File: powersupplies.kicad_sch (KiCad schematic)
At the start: 24 parts, among them U1 OB2222M, U2 LM317L_SOT-89

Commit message: All parts on. Set foots for everything. Time to try a layout.
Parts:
- C1, C2, C9: footprint (none) -> Capacitor_SMD:C_0603_1608Metric
- C11, C12: footprint (none) -> Capacitor_SMD:C_0402_1005Metric
- C3: footprint (none) -> Capacitor_SMD:C_0805_2012Metric
- C5, C6, C7: footprint (none) -> Capacitor_THT:CP_Radial_D6.3mm_P2.50mm
- D1, D3: footprint (none) -> Diode_SMD:D_SMF
- D2, D5: footprint (none) -> Diode_SMD:D_SOD-123F
- L1: footprint (none) -> Inductor_THT:L_Axial_L9.5mm_D4.0mm_P5.08mm_Vertical_Fastron_SMCC
- L2: footprint (none) -> Inductor_THT:L_Radial_D8.7mm_P5.00mm_Fastron_07HCP
- R1, R3: footprint (none) -> Resistor_SMD:R_0805_2012Metric
- R2, R26, R4, R9: footprint (none) -> Resistor_SMD:R_0603_1608Metric
- R5: footprint (none) -> Resistor_SMD:R_1206_3216Metric
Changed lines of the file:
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@@
 			)
 		)
-		(property "Footprint" ""
+		(property "Footprint" "Capacitor_SMD:C_0805_2012Metric"
 			(at 100.0252 59.69 0)
 			(effects
@@
 			)
 		)
-		(property "Footprint" ""
+		(property "Footprint" "Resistor_SMD:R_0805_2012Metric"
 			(at 92.456 48.006 90)
 			(effects
@@
 			)
 		)
-		(property "Footprint" ""
+		(property "Footprint" "Diode_SMD:D_SOD-123F"
 			(at 40.64 71.12 0)
 			(effects
@@
 			)
 		)
-		(property "Footprint" ""
+		(property "Footprint" "Diode_SMD:D_SMF"
 			(at 139.7 91.44 0)
 			(effects
@@
 			)
 		)
-		(property "Footprint" ""
+		(property "Footprint" "Capacitor_THT:CP_Radial_D6.3mm_P2.50mm"
 			(at 73.66 80.01 0)
 			(effects
@@
 			)
 		)
-		(property "Footprint" ""
+		(property "Footprint" "Capacitor_SMD:C_0603_1608Metric"
 			(at 186.9948 143.51 0)
 			(effects
@@
 			)
 		)
-		(property "Footprint" ""
+		(property "Footprint" "Capacitor_SMD:C_0603_1608Metric"
 			(at 145.0848 73.66 0)
 			(effects
@@
 			)
 		)
-		(property "Footprint" ""
+		(property "Footprint" "Diode_SMD:D_SMF"
 			(at 157.48 71.12 0)
 			(effects
@@
 			)
 		)
-		(property "Footprint" ""
+		(property "Footprint" "Inductor_THT:L_Axial_L9.5mm_D4.0mm_P5.08mm_Vertical_Fastron_SMCC"
 			(at 67.31 71.12 0)
 			(effects
@@
 			)
 		)
-		(property "Footprint" ""
+		(property "Footprint" "Capacitor_THT:CP_Radial_D6.3mm_P2.50mm"
 			(at 167.64 91.44 0)
 			(effects
@@
 			)
 		)
-		(property "Footprint" ""
+		(property "Footprint" "Capacitor_SMD:C_0603_1608Metric"
 			(at 131.7752 81.28 0)
 			(effects
@@
 			)
 		)
-		(property "Footprint" ""
+		(property "Footprint" "Resistor_SMD:R_0603_1608Metric"
 			(at 139.954 70.104 90)
 			(effects
@@
 			)
 		)
-		(property "Footprint" ""
+		(property "Footprint" "Resistor_SMD:R_1206_3216Metric"
 			(at 125.476 77.724 90)
 			(effects
@@
 			)
 		)
-		(property "Footprint" ""
+		(property "Footprint" "Resistor_SMD:R_0603_1608Metric"
 			(at 149.606 58.674 90)
 			(effects
@@
 			)
 		)
-		(property "Footprint" ""
+		(property "Footprint" "Resistor_SMD:R_0805_2012Metric"
 			(at 81.534 60.706 90)
 			(effects
@@
 			)
 		)
-		(property "Footprint" ""
+		(property "Footprint" "Resistor_SMD:R_0603_1608Metric"
 			(at 177.546 147.574 90)
 			(effects
@@
 			)
 		)
-		(property "Footprint" ""
+		(property "Footprint" "Diode_SMD:D_SOD-123F"
 			(at 52.07 71.12 0)
 			(effects
@@
 			)
 		)
-		(property "Footprint" ""
+		(property "Footprint" "Capacitor_THT:CP_Radial_D6.3mm_P2.50mm"
 			(at 58.42 80.01 0)
 			(effects
@@
 			)
 		)
-		(property "Footprint" ""
+		(property "Footprint" "Inductor_THT:L_Radial_D8.7mm_P5.00mm_Fastron_07HCP"
 			(at 157.48 85.09 0)
 			(effects
@@
 			)
 		)
-		(property "Footprint" ""
+		(property "Footprint" "Resistor_SMD:R_0603_1608Metric"
 			(at 200.914 128.524 90)
 			(effects
@@
 			)
 		)
-		(property "Footprint" ""
+		(property "Footprint" "Capacitor_SMD:C_0402_1005Metric"
 			(at 226.3648 143.51 0)
 			(effects
@@
 			)
 		)
-		(property "Footprint" ""
+		(property "Footprint" "Capacitor_SMD:C_0402_1005Metric"
 			(at 214.9348 143.51 0)
 			(effects

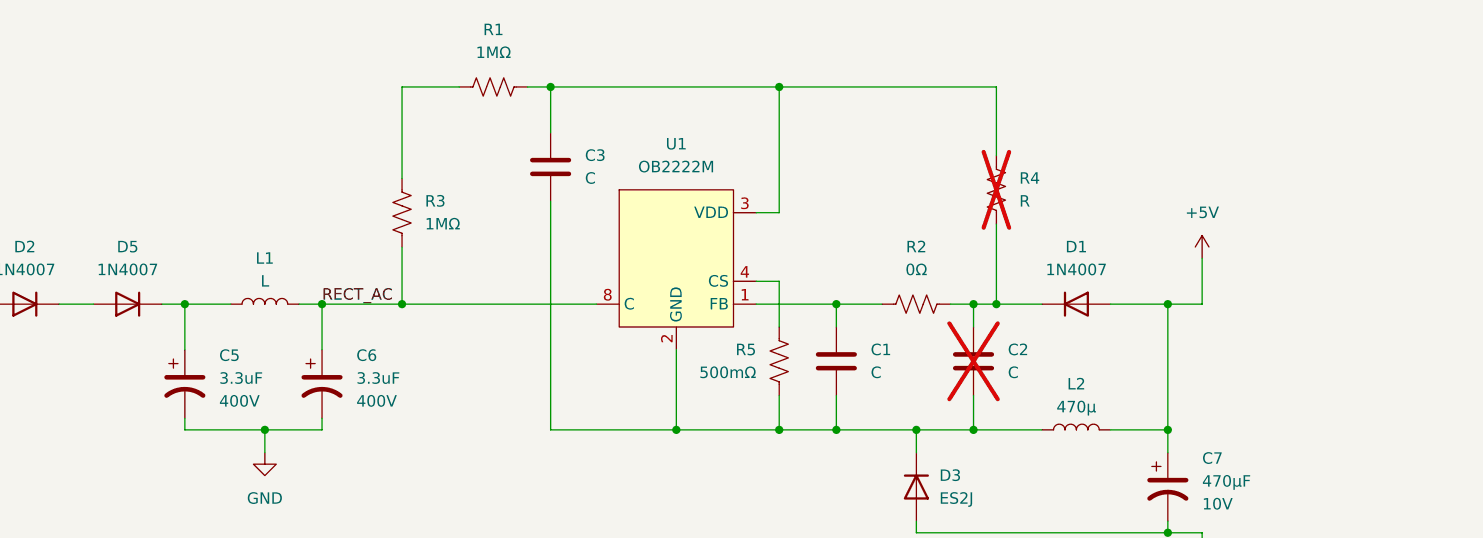
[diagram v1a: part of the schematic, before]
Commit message: Made a first board layout.
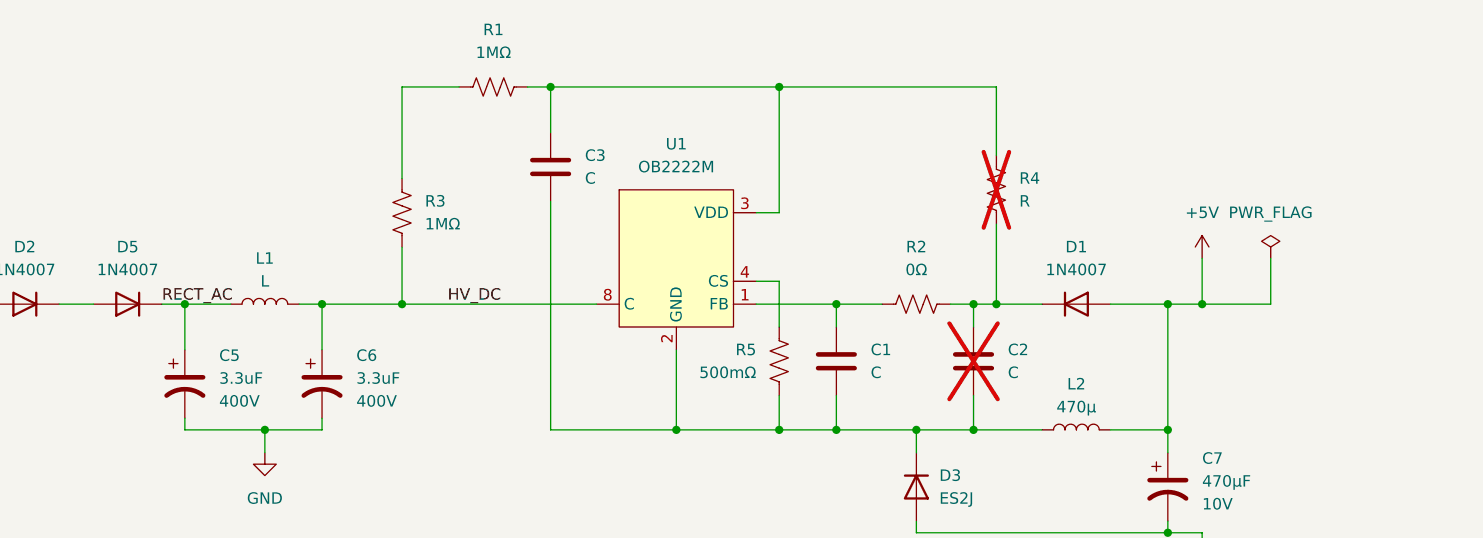
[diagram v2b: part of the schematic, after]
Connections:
- net RECT_AC: now reaches C5.1, D5.1 (K), L1.1
- net C renamed HV_DC
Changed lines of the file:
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@@
+	)
+	(junction
+		(at 171.45 71.12)
+		(diameter 0)
+		(color 0 0 0 0)
 	)
 	(junction
@@
 	(wire
 		(pts
+			(xy 179.07 71.12) (xy 179.07 66.04)
+		)
+		(stroke
+			(width 0)
+			(type default)
+		)
+	)
+	(wire
+		(pts
 			(xy 82.55 46.99) (xy 88.9 46.99)
 		)
@@
 		)
 	)
+	(wire
+		(pts
+			(xy 171.45 71.12) (xy 179.07 71.12)
+		)
+		(stroke
+			(width 0)
+			(type default)
+		)
+	)
 	(label "RECT_AC"
-		(at 73.66 71.12 0)
+		(at 55.88 71.12 0)
+		(effects
+			(font
+				(size 1.27 1.27)
+			)
+			(justify left bottom)
+		)
+	)
+	(label "HV_DC"
+		(at 87.63 71.12 0)
 		(effects
 			(font
@@
 					(unit 1)
 				)
+			)
+		)
+	)
+	(symbol
+		(lib_id "power:PWR_FLAG")
+		(at 179.07 66.04 0)
+		(unit 1)
+		(exclude_from_sim no)
+		(in_bom yes)
+		(on_board yes)
+		(dnp no)
+		(fields_autoplaced yes)
+		(property "Reference" "#FLG03"
+			(at 179.07 64.135 0)
+			(effects
+				(font
+					(size 1.27 1.27)
+				)
+				(hide yes)
+			)
+		)
+		(property "Value" "PWR_FLAG"
+			(at 179.07 60.96 0)
+			(effects
+				(font
+					(size 1.27 1.27)
+				)
+			)
+		)
+		(property "Footprint" ""
+			(at 179.07 66.04 0)
+			(effects
+				(font
+					(size 1.27 1.27)
+				)
+				(hide yes)
+			)
+		)
+		(property "Datasheet" "~"
+			(at 179.07 66.04 0)
+			(effects
+				(font
+					(size 1.27 1.27)
+				)
+				(hide yes)
+			)
+		)
+		(property "Description" "Special symbol for telling ERC where power comes from"
+			(at 179.07 66.04 0)
+			(effects
+				(font
+					(size 1.27 1.27)
+				)
+				(hide yes)
+			)
+		)
+		(pin "1"
+		)
+		(instances
+			(project ""
+				(path "/0b789f5a-74d1-4f81-bd1f-7ac838c6392e/fc2455a2-d0e8-4734-8077-69cf72fecbb3"
+					(reference "#FLG03")
+					(unit 1)
+				)

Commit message: Have a full board layout which resembles the original in some ways. Made a few schematic fixes to match better.
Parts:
- L1: footprint Inductor_THT:L_Axial_L9.5mm_D4.0mm_P5.08mm_Vertical_Fastron_SMCC -> HF relays:L_Axial_L9.5mm_D4.0mm_P3.81mm_Vertical
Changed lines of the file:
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@@
 			)
 		)
-		(property "Footprint" "Inductor_THT:L_Axial_L9.5mm_D4.0mm_P5.08mm_Vertical_Fastron_SMCC"
+		(property "Footprint" "HF relays:L_Axial_L9.5mm_D4.0mm_P3.81mm_Vertical"
 			(at 67.31 71.12 0)
 			(effects

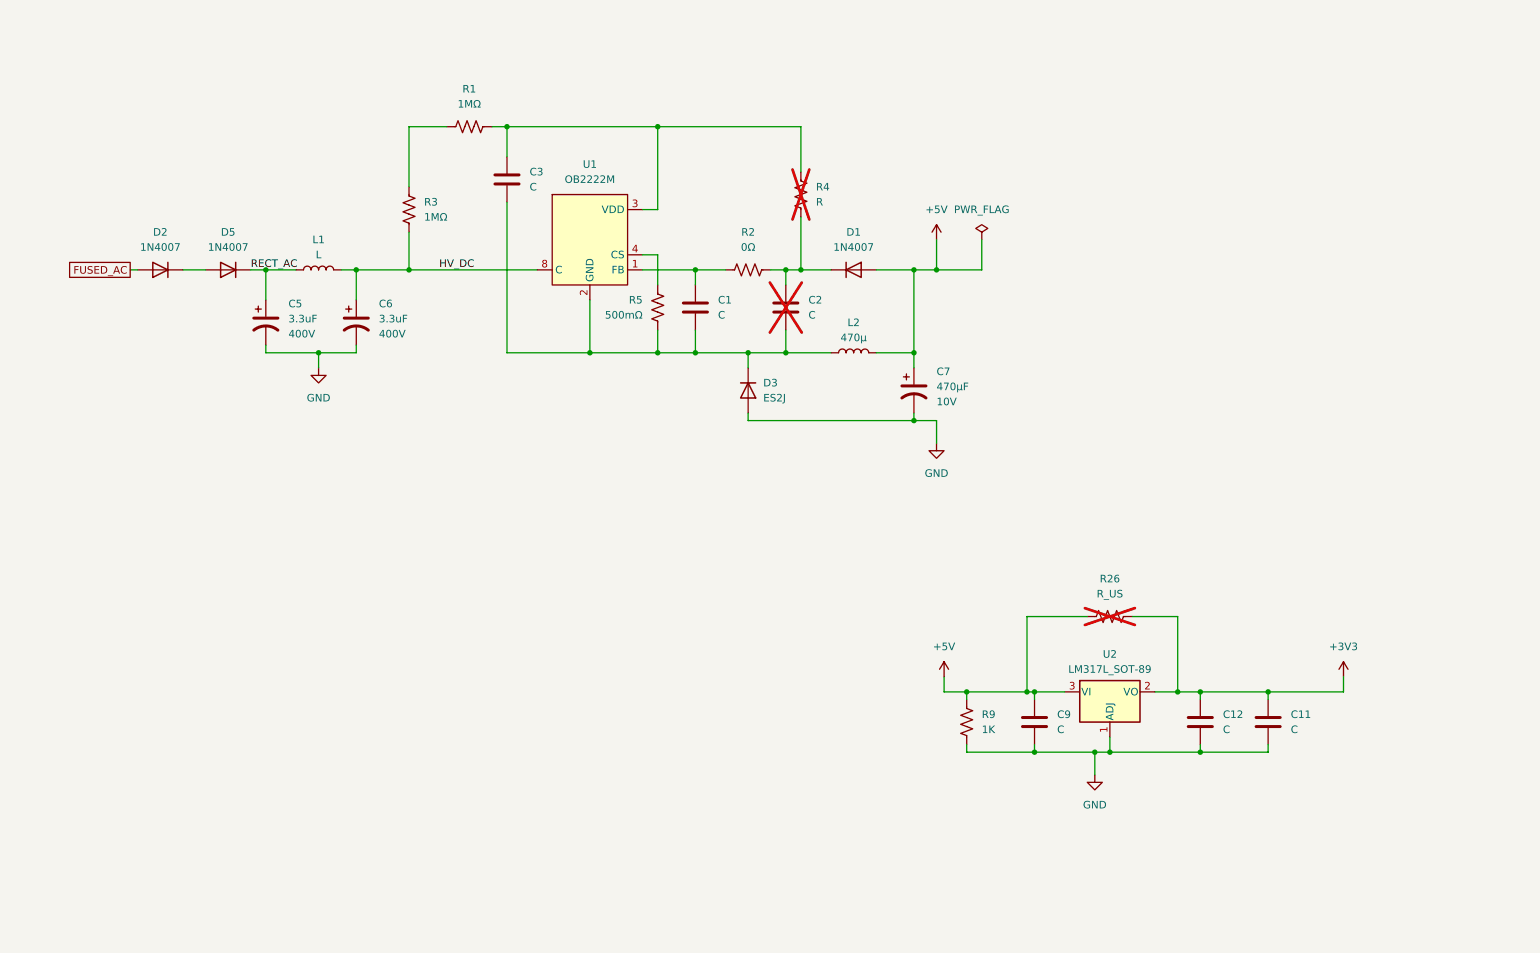
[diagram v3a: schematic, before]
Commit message: Making board layout match better. Added new footprints and symbols.
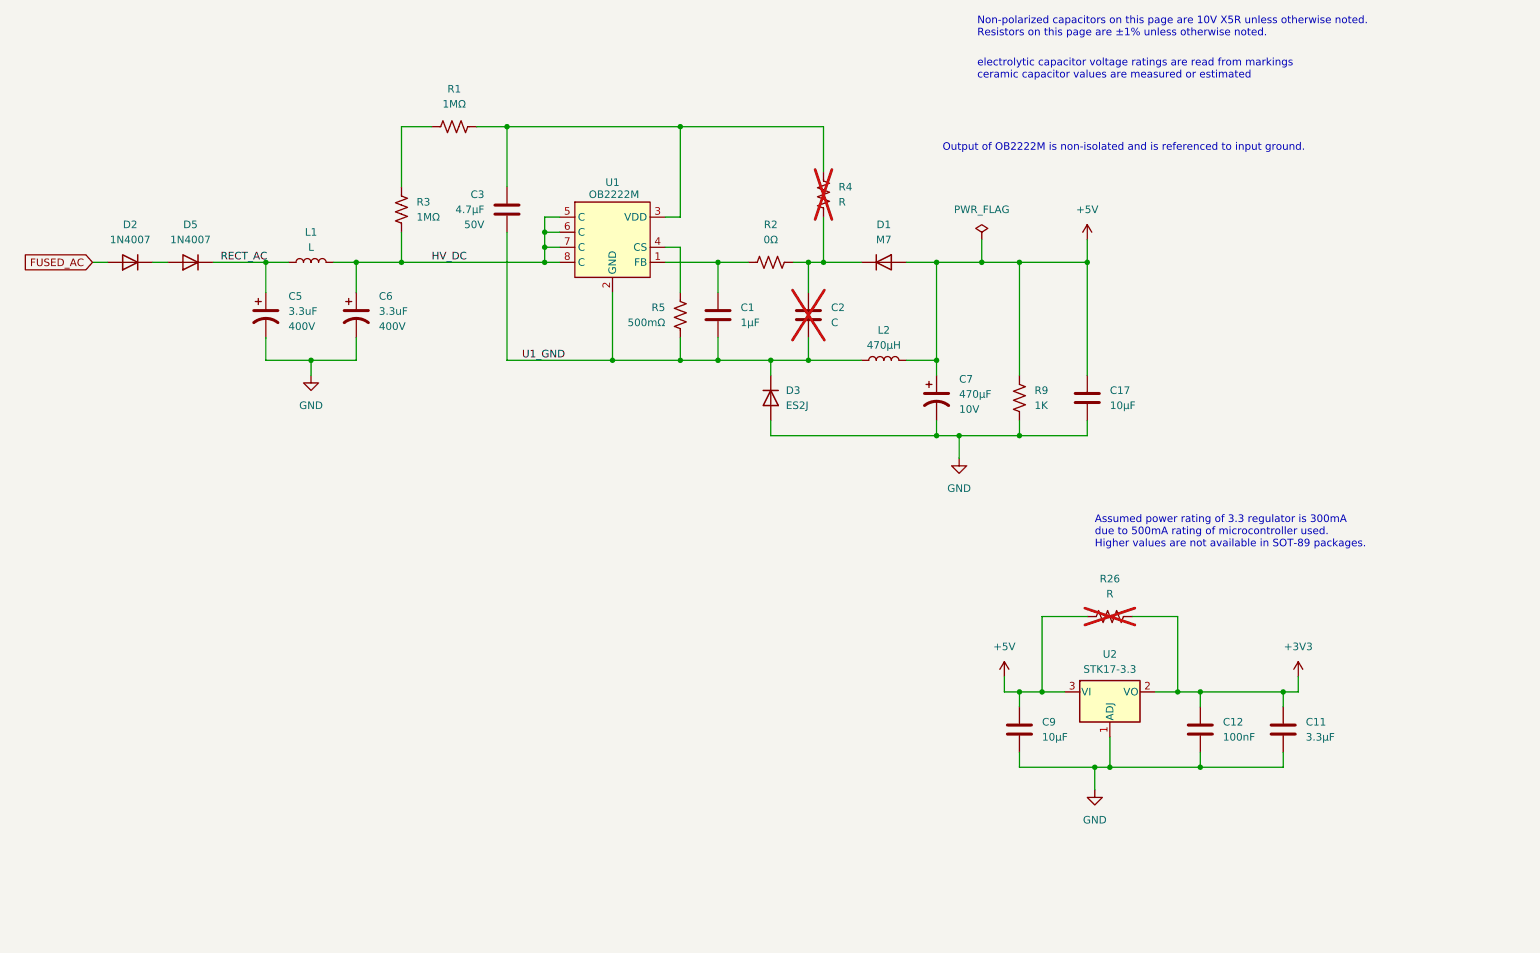
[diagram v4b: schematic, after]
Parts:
- added C17: 10µF, Capacitor_SMD:C_0603_1608Metric, symbol Device:C
- C1: value C -> 1µF
- C11: value C -> 3.3µF
- C12: value C -> 100nF
- C3: value C -> 4.7µF; Voltage (none) -> 50V
- C9: value C -> 10µF
- D1: value 1N4007 -> M7; footprint Diode_SMD:D_SMF -> Diode_SMD:D_SMA
- D3: footprint Diode_SMD:D_SMF -> Diode_SMD:D_SMA
- L2: value 470µ -> 470µH
- R26: value R_US -> R
- U2: value LM317L_SOT-89 -> STK17-3.3
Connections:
- net +5V: now also C17.1
- net GND: now also C17.2
- net U1_GND: now reaches C1.2, C2.1, C3.2, D3.1 (K), L2.1, R5.2, U1.2 (GND)
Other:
- note added: "Assumed power rating of 3.3 regulator is 300mA due to 500mA rating of microcontroller used. Higher values are not available in SOT-89 packages."
- note added: "Non-polarized capacitors on this page are 10V X5R unless otherwise noted. Resistors on this page are ±1% unless otherwise noted."
- note added: "Output of OB2222M is non-isolated and is referenced to input ground."
- note added: "electrolytic capacitor voltage ratings are read from markings ceramic capacitor values are measured or estimated"
- title: (none) -> power supplies
- moved on the sheet: C1, C11, C12, C2, C3, C5, C6, C7, C9, D1, D2, D3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
